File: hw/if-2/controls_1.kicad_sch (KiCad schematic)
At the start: 0 parts

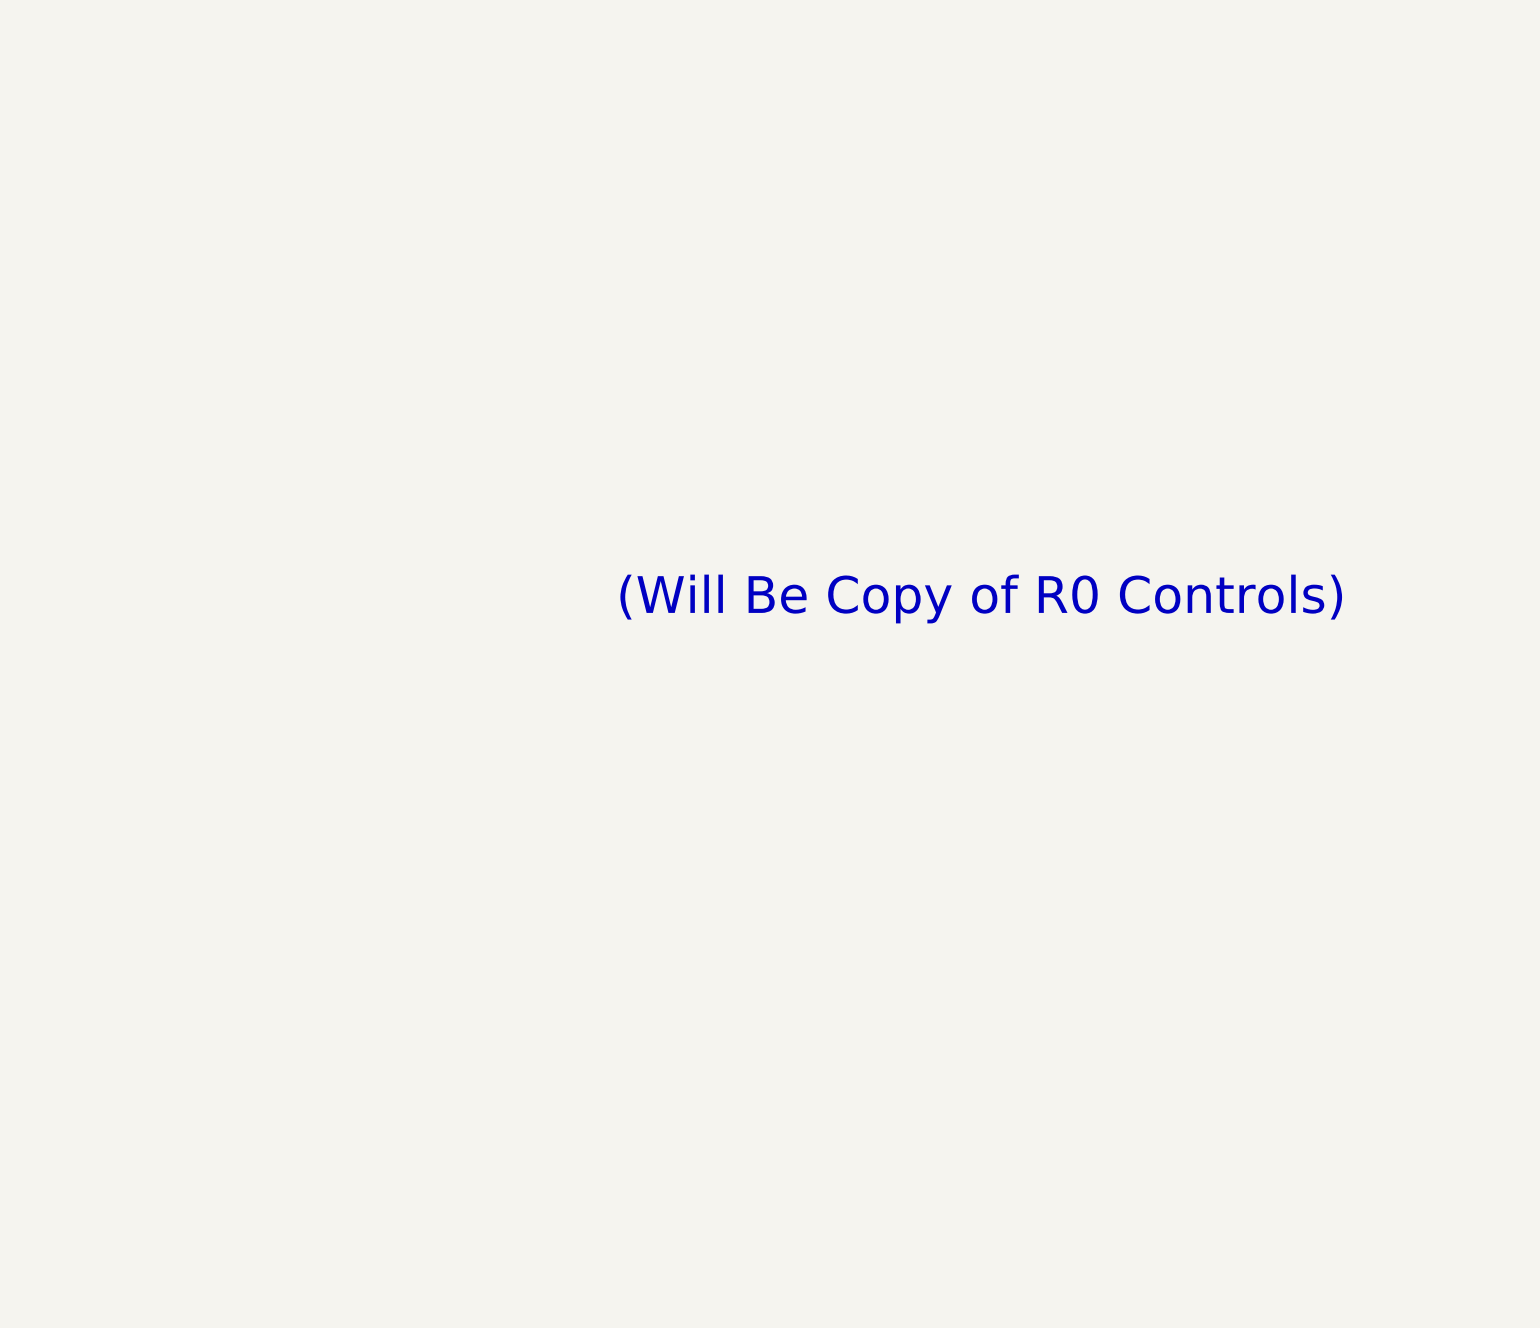
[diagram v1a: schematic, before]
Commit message: Ready to do layout on IF2 board
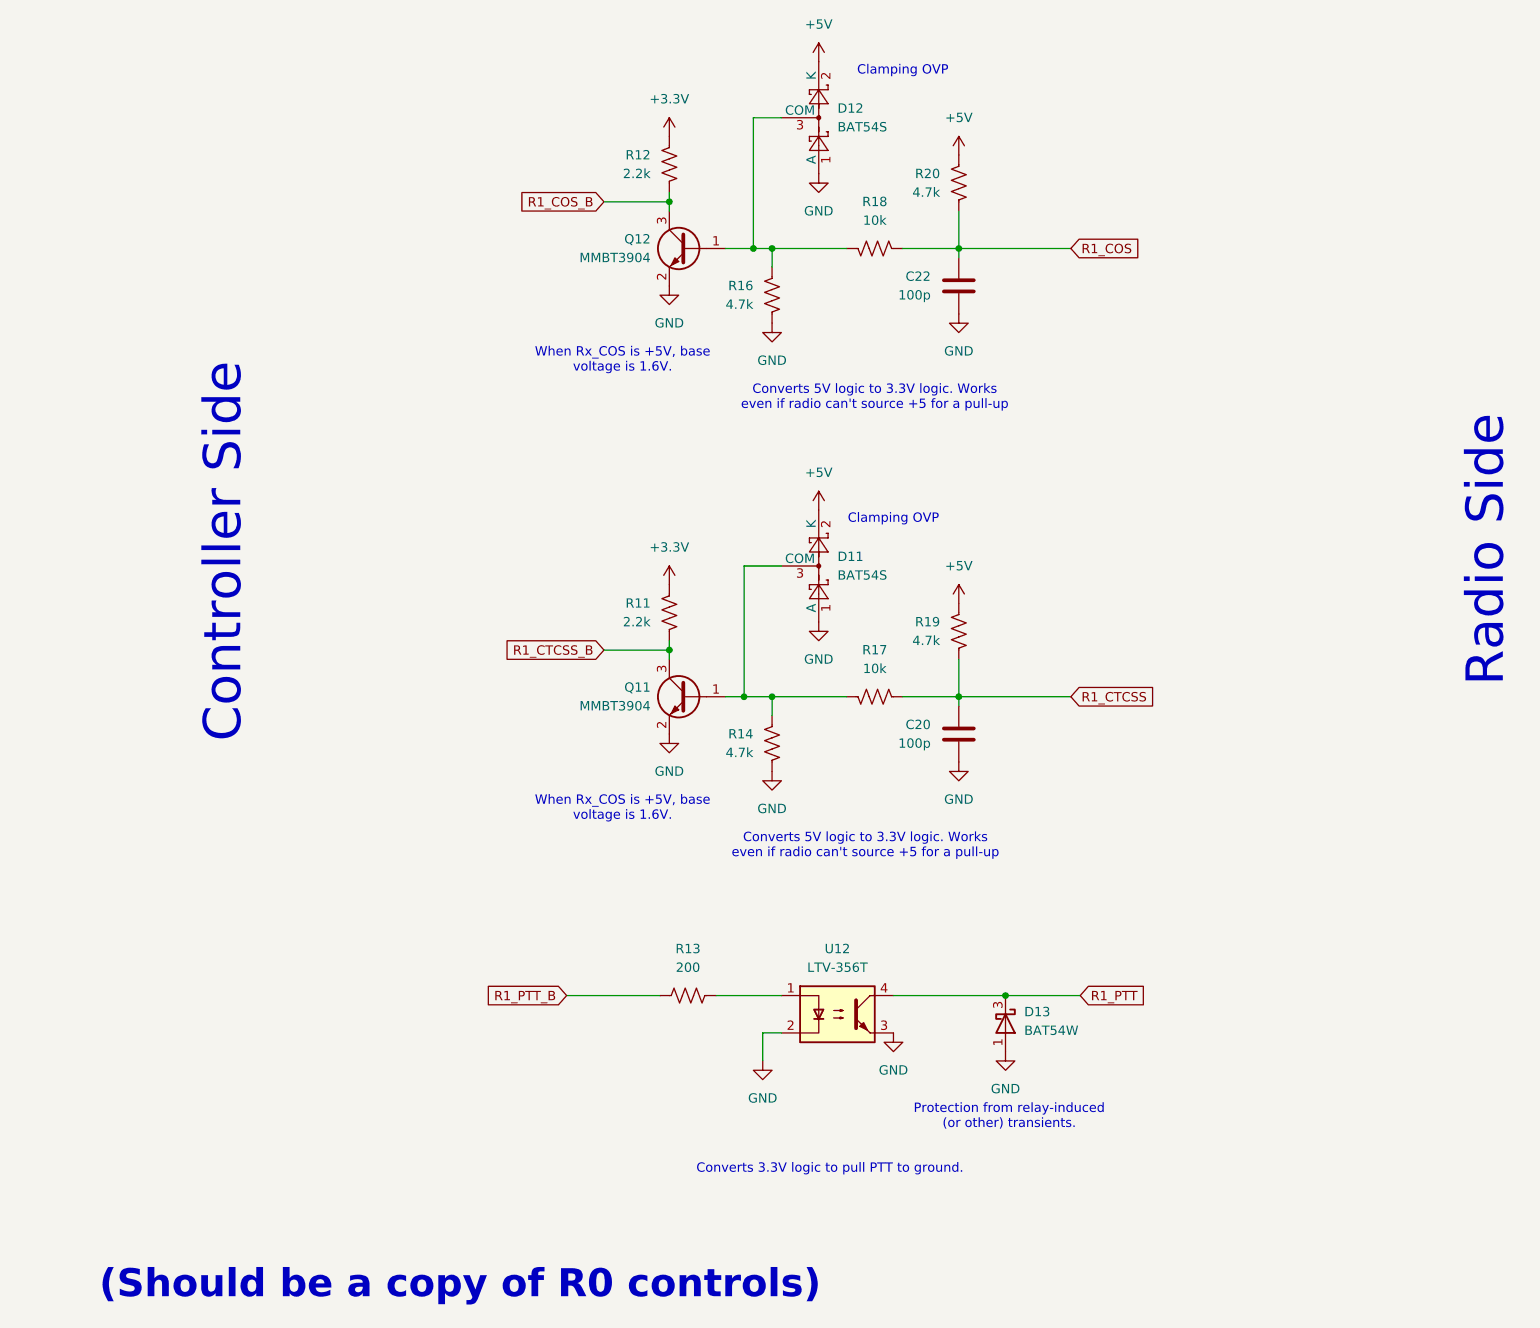
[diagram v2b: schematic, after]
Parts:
- added C20, C22: 100p, Capacitor_SMD:C_0805_2012Metric_Pad1.18x1.45mm_HandSolder, symbol Device:C
- added D11, D12: BAT54S, Package_TO_SOT_SMD:SOT-23, symbol Diode:BAT54S
- added D13: BAT54W, Package_TO_SOT_SMD:SOT-323_SC-70, symbol Diode:BAT54W
- added Q11, Q12: MMBT3904, Package_TO_SOT_SMD:SOT-23, symbol Transistor_BJT:MMBT3904
- added R11, R12: 2.2k, Resistor_SMD:R_0805_2012Metric_Pad1.20x1.40mm_HandSolder, symbol Device:R_US
- added R13: 200, Resistor_SMD:R_0805_2012Metric_Pad1.20x1.40mm_HandSolder, symbol Device:R_US
- added R14, R16, R19, R20: 4.7k, Resistor_SMD:R_0805_2012Metric_Pad1.20x1.40mm_HandSolder, symbol Device:R_US
- added R17, R18: 10k, Resistor_SMD:R_0805_2012Metric_Pad1.20x1.40mm_HandSolder, symbol Device:R_US
- added U12: LTV-356T, Package_SO:SO-4_4.4x3.6mm_P2.54mm, symbol Isolator:LTV-356T
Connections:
- new net: D12.3 (COM), Q12.1 (B), R16.1, R18.2
- new net: D11.3 (COM), Q11.1 (B), R14.1, R17.2
- new net: R13.2, U12.1
- new net +3.3V: R11.1, R12.1
- new net +5V: D11.2 (K), D12.2 (K), R19.1, R20.1
- new net GND: C20.2, C22.2, D11.1 (A), D12.1 (A), D13.1 (A), Q11.2 (E), Q12.2 (E), R14.2, R16.2, U12.2, U12.3
- new net R1_COS: C22.1, R18.1, R20.2
- new net R1_COS_B: Q12.3 (C), R12.2
- new net R1_CTCSS: C20.1, R17.1, R19.2
- new net R1_CTCSS_B: Q11.3 (C), R11.2
- new net R1_PTT: D13.3 (K), U12.4
- new net R1_PTT_B: R13.1
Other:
- note added: "(Should be a copy of R0 controls)"
- note added: "Clamping OVP"
- note added: "Controller Side"
- note added: "Converts 3.3V logic to pull PTT to ground."
- note added: "Converts 5V logic to 3.3V logic. Works even if radio can't source +5 for a pull-up"
- note added: "Protection from relay-induced (or other) transients."
- note added: "Radio Side"
- note added: "When Rx_COS is +5V, base voltage is 1.6V."
- note removed: "(Will Be Copy of R0 Controls)"
- title: (none) -> COS/CTCSS/PTT Controls (Radio 1)

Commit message: Making progress on layout
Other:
- moved on the sheet: C20, C22, D11, D12, D13, Q11, Q12, R11, R12, R13, R14, R16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
